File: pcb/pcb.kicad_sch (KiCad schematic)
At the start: 34 parts, among them J1 Conn_01x20, J10 Conn_01x03, J11 Conn_01x03, J12 Conn_01x03, J2 Conn_01x20, J3 Conn_01x20, J4 Conn_01x20, J5 Conn_01x20, J6 Conn_01x20, J7 Conn_01x20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

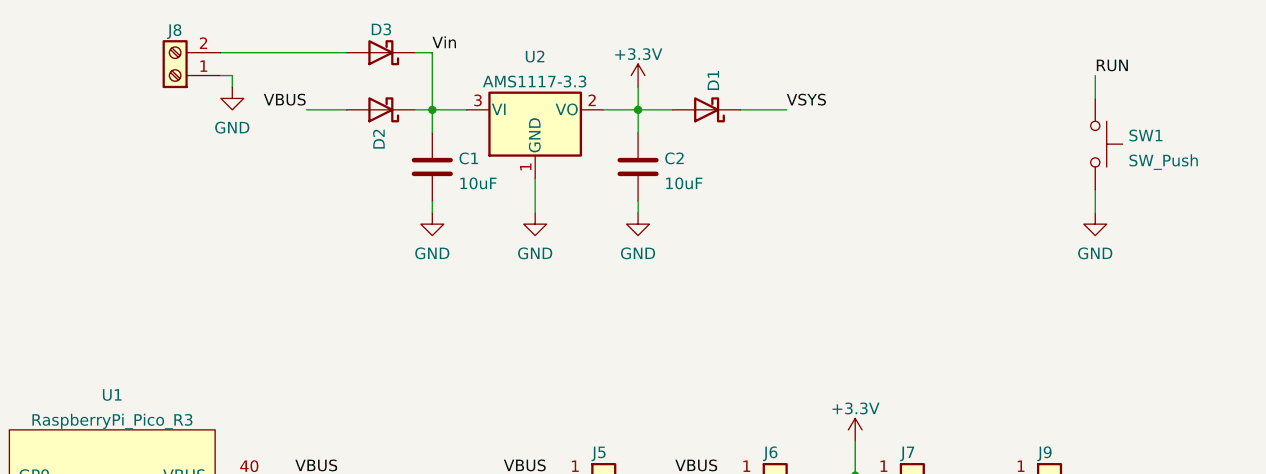
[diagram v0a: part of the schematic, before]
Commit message: add schematic PDF
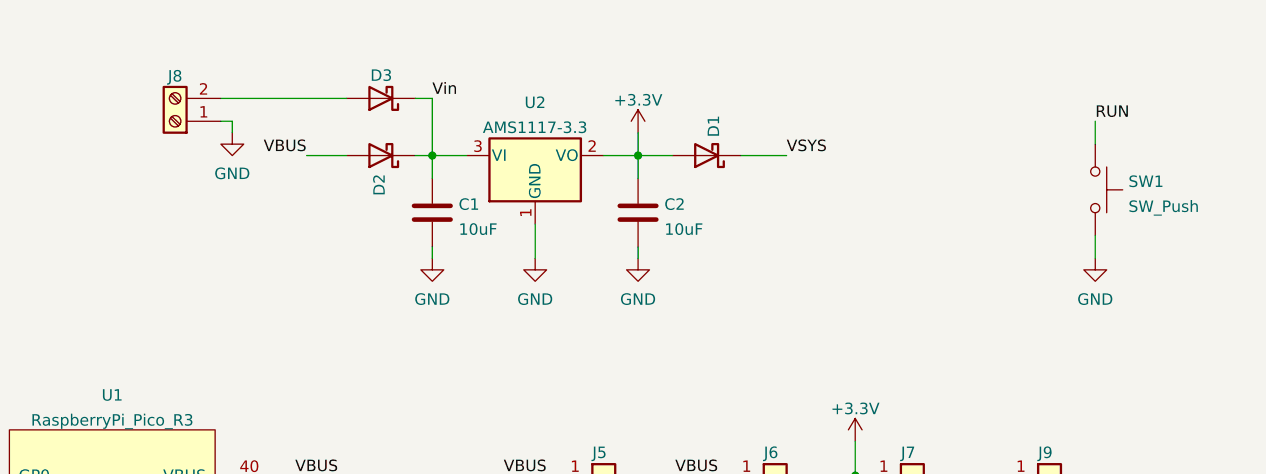
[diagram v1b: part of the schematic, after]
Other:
- company: (none) -> Core Electronics
- title: (none) -> Makerverse Breakout Board for Raspberry Pi Pico
- moved on the sheet: C1, C2, D1, D2, D3, J8, SW1, U2
